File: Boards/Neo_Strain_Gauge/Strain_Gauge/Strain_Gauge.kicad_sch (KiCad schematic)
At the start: 49 parts, among them J1 Screw_Terminal_01x03, J2 Screw_Terminal_01x03, J3 Screw_Terminal_01x03, J4 Screw_Terminal_01x03, J5 Conn_01x02, J6 USB_B_Micro, U1 W25Q128JVS, U2 NCP1117-3.3_SOT223, U3 LTC2344IUH-16-PBF, U4 RP2040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

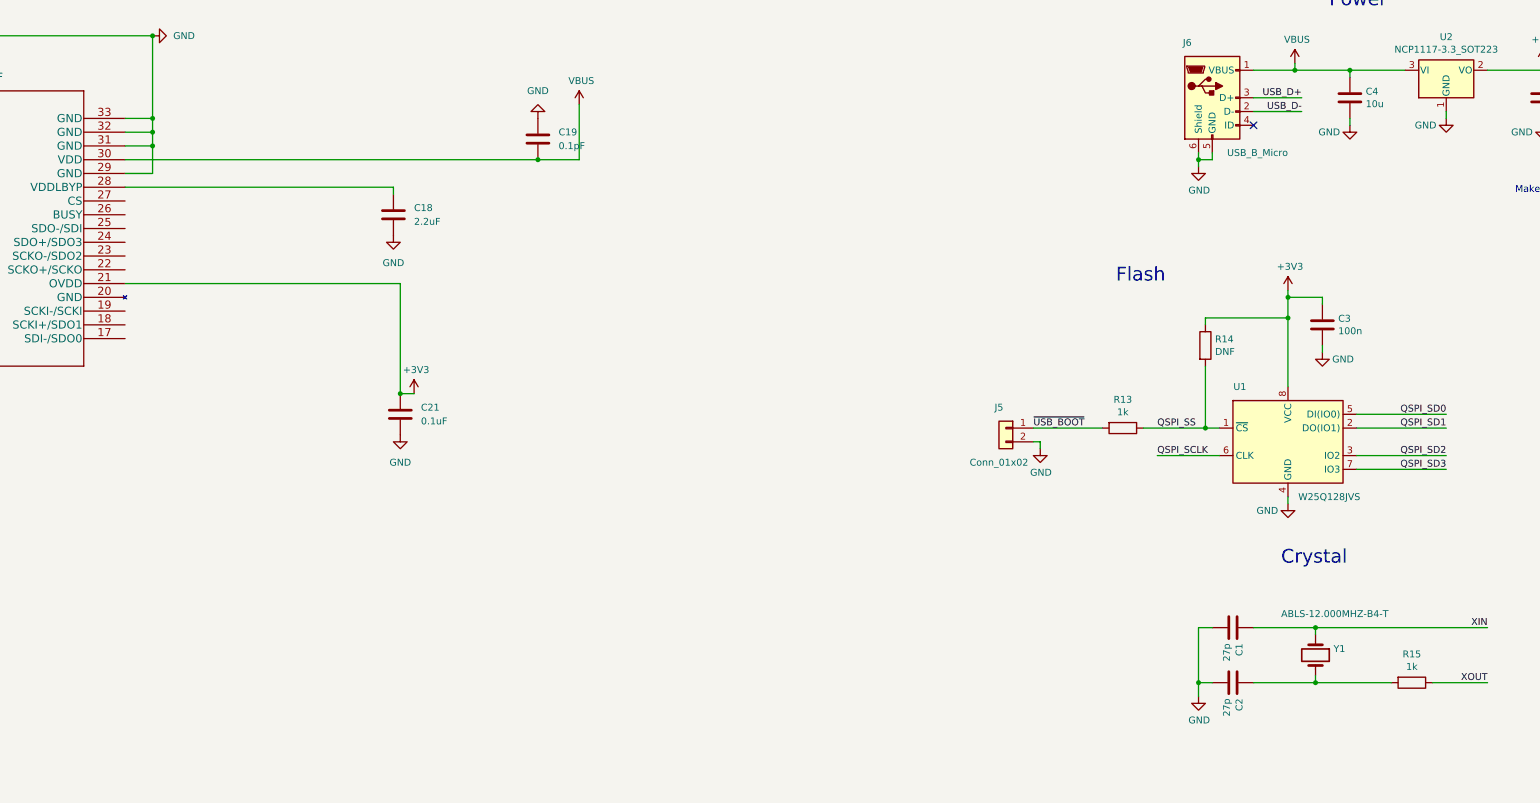
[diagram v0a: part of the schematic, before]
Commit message: Added schematic changes to pull in the mainboard
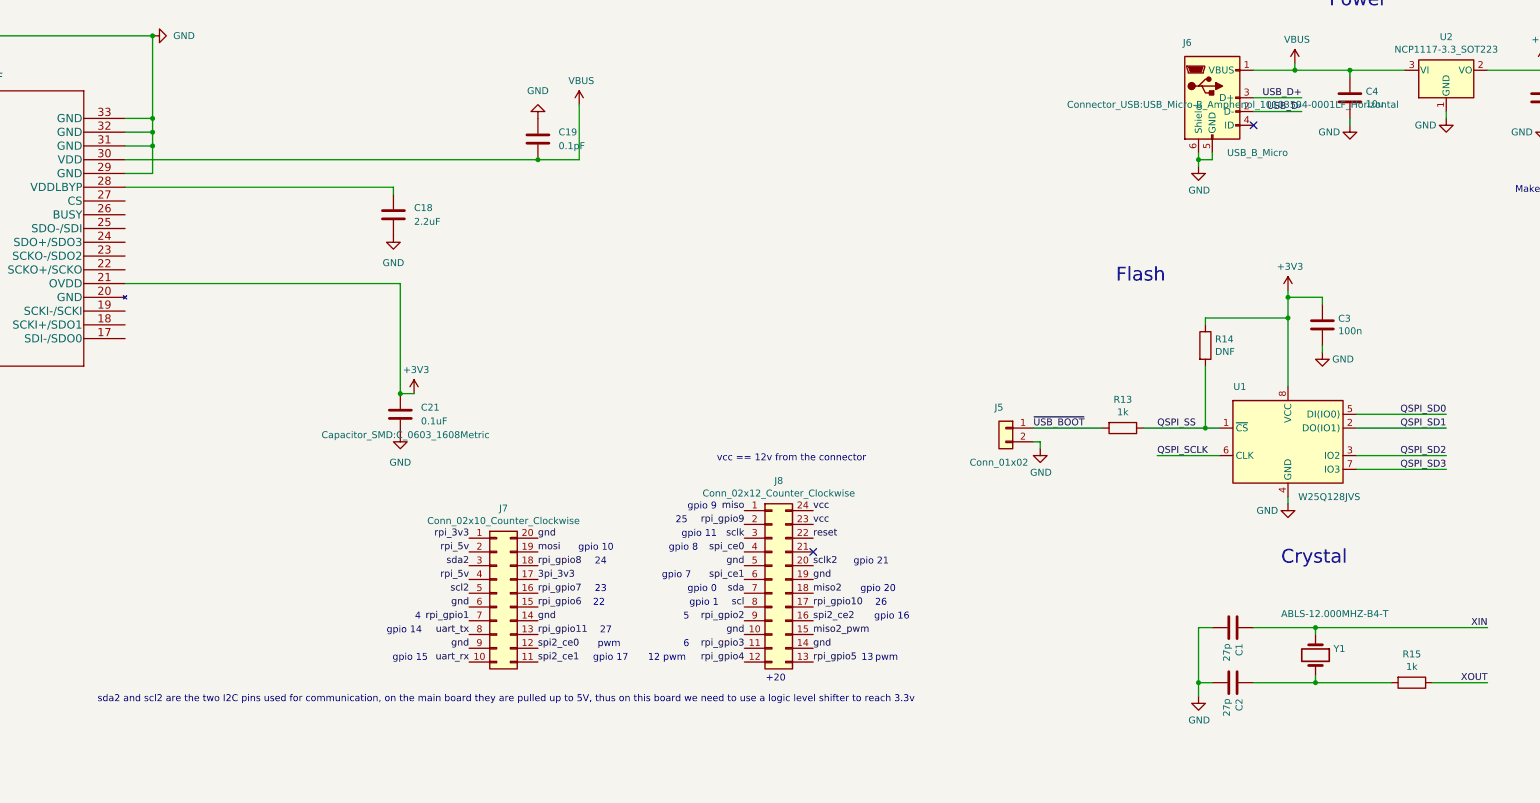
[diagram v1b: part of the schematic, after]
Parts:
- added J7: Conn_02x10_Counter_Clockwise, Connector_PinHeader_2.54mm:PinHeader_2x10_P2.54mm_Vertical, symbol Connector_Generic:Conn_02x10_Counter_Clockwise
- added J8: Conn_02x12_Counter_Clockwise, Connector_PinHeader_2.54mm:PinHeader_2x12_P2.54mm_Vertical, symbol Connector_Generic:Conn_02x12_Counter_Clockwise
- C18, C20: footprint Capacitor_SMD:C_0201_0603Metric -> Capacitor_SMD:C_0603_1608Metric
- C19, C21: footprint (none) -> Capacitor_SMD:C_0603_1608Metric
- J6: footprint RP2040_minimal:USB_Micro-B_Amphenol_10103594-0001LF_Horizontal_modified -> Connector_USB:USB_Micro-B_Amphenol_10103594-0001LF_Horizontal
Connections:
- new net 3pi_3v3: J7.17 (Pin_17)
- new net gnd: J7.14 (Pin_14), J7.20 (Pin_20), J7.6 (Pin_6), J7.9 (Pin_9), J8.10 (Pin_10), J8.14 (Pin_14), J8.19 (Pin_19), J8.5 (Pin_5)
- new net miso: J8.1 (Pin_1)
- new net miso2: J8.18 (Pin_18)
- new net miso2_pwm: J8.15 (Pin_15)
- new net mosi: J7.19 (Pin_19)
- new net reset: J8.22 (Pin_22)
- new net rpi_3v3: J7.1 (Pin_1)
- new net rpi_5v: J7.2 (Pin_2), J7.4 (Pin_4)
- new net rpi_gpio1: J7.7 (Pin_7)
- new net rpi_gpio10: J8.17 (Pin_17)
- new net rpi_gpio11: J7.13 (Pin_13)
- new net rpi_gpio2: J8.9 (Pin_9)
- new net rpi_gpio3: J8.11 (Pin_11)
- new net rpi_gpio4: J8.12 (Pin_12)
- new net rpi_gpio5: J8.13 (Pin_13)
- new net rpi_gpio6: J7.15 (Pin_15)
- new net rpi_gpio7: J7.16 (Pin_16)
- new net rpi_gpio8: J7.18 (Pin_18)
- new net rpi_gpio9: J8.2 (Pin_2)
- new net scl: J8.8 (Pin_8)
- new net scl2: J7.5 (Pin_5)
- new net sclk: J8.3 (Pin_3)
- new net sclk2: J8.20 (Pin_20)
- new net sda: J8.7 (Pin_7)
- new net sda2: J7.3 (Pin_3)
- new net spi2_ce0: J7.12 (Pin_12)
- new net spi2_ce1: J7.11 (Pin_11)
- new net spi2_ce2: J8.16 (Pin_16)
- new net spi_ce0: J8.4 (Pin_4)
- new net spi_ce1: J8.6 (Pin_6)
- new net uart_rx: J7.10 (Pin_10)
- new net uart_tx: J7.8 (Pin_8)
- new net vcc: J8.23 (Pin_23), J8.24 (Pin_24)
- no-connect marks 1 -> 2
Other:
- note added: "+20"
- note added: "12 pwm"
- note added: "13"
- note added: "22"
- note added: "23"
- note added: "24"
- note added: "25"
- note added: "26"
- note added: "27"
- note added: "4"
- note added: "5"
- note added: "6"
- note added: "gpio 0"
- note added: "gpio 1"
- note added: "gpio 10"
- note added: "gpio 11"
- note added: "gpio 14"
- note added: "gpio 15"
- note added: "gpio 16"
- note added: "gpio 17"
- note added: "gpio 20"
- note added: "gpio 21"
- note added: "gpio 7"
- note added: "gpio 8"
- note added: "gpio 9"
- note added: "pwm"
- note added: "sda2 and scl2 are the two I2C pins used for communication, on the main board they are pulled up to 5V, thus on this board we need to use a logic level shifter to reach 3.3v"
- note added: "vcc == 12v from the connector"

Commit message: 0603 more things
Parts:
- C3: footprint Capacitor_SMD:C_0402_1005Metric -> Capacitor_SMD:C_0603_1608Metric
- C4: footprint Capacitor_SMD:C_0805_2012Metric -> Capacitor_SMD:C_0603_1608Metric
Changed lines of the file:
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@@
       (effects (font (size 1.27 1.27)) (justify left))
     )
-    (property "Footprint" "Capacitor_SMD:C_0402_1005Metric" (id 2) (at 247.3452 313.69 0)
+    (property "Footprint" "Capacitor_SMD:C_0603_1608Metric" (id 2) (at 247.3452 313.69 0)
       (effects (font (size 1.27 1.27)) hide)
     )
@@
       (effects (font (size 1.27 1.27)) (justify left))
     )
-    (property "Footprint" "Capacitor_SMD:C_0805_2012Metric" (id 2) (at 252.4252 271.78 0)
+    (property "Footprint" "Capacitor_SMD:C_0603_1608Metric" (id 2) (at 252.4252 271.78 0)
       (effects (font (size 1.27 1.27)) hide)
     )
@@
     )
     (path "/071334f5-4350-4cd7-bf23-5922b5c00fab"
-      (reference "C3") (unit 1) (value "100n") (footprint "Capacitor_SMD:C_0402_1005Metric")
+      (reference "C3") (unit 1) (value "100n") (footprint "Capacitor_SMD:C_0603_1608Metric")
     )
     (path "/d0a1192c-a07d-40a6-a7b0-dc33661cf95a"
-      (reference "C4") (unit 1) (value "10u") (footprint "Capacitor_SMD:C_0805_2012Metric")
+      (reference "C4") (unit 1) (value "10u") (footprint "Capacitor_SMD:C_0603_1608Metric")
     )
     (path "/88bc9d99-afa2-40e7-b578-1b4cda291bf5"

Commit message: Add current work
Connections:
- net GND: now also J7.14 (Pin_14), J7.20 (Pin_20), J7.6 (Pin_6), J8.10 (Pin_10), J8.14 (Pin_14), J8.19 (Pin_19), J8.5 (Pin_5)
- net gnd: no longer J7.14 (Pin_14), J7.20 (Pin_20), J7.6 (Pin_6), J8.10 (Pin_10), J8.14 (Pin_14), J8.19 (Pin_19), J8.5 (Pin_5)
- no-connect marks 2 -> 3
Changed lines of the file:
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@@
   (junction (at -44.45 292.1) (diameter 0) (color 0 0 0 0)
   )
+  (junction (at 124.46 364.49) (diameter 0) (color 0 0 0 0)
+  )
   (junction (at 441.96 264.16) (diameter 0) (color 0 0 0 0)
   )
+  (junction (at 124.46 354.33) (diameter 0) (color 0 0 0 0)
+  )
   (junction (at 223.52 375.92) (diameter 0) (color 0 0 0 0)
   )
@@
   (junction (at 419.1 275.59) (diameter 0) (color 0 0 0 0)
   )
+  (junction (at 167.64 356.87) (diameter 0) (color 0 0 0 0)
+  )
   (junction (at 251.46 262.89) (diameter 0) (color 0 0 0 0)
   )
@@
   )
   (no_connect (at 233.68 273.05))
+  (no_connect (at 707.39 374.65))
   (no_connect (at 152.4 351.79))
   (wire (pts (xy 365.76 297.18) (xy 365.76 284.48))
@@
     (stroke (width 0) (type default) (color 0 0 0 0))
   )
+  (wire (pts (xy 101.6 364.49) (xy 124.46 364.49))
+    (stroke (width 0) (type default) (color 0 0 0 0))
+  )
   (wire (pts (xy 226.06 365.76) (xy 223.52 365.76))
     (stroke (width 0) (type default) (color 0 0 0 0))
@@
     (stroke (width 0) (type default) (color 0 0 0 0))
   )
+  (wire (pts (xy 167.64 356.87) (xy 170.18 356.87))
+    (stroke (width 0) (type default) (color 0 0 0 0))
+  )
   (wire (pts (xy 391.16 358.14) (xy 406.4 358.14))
     (stroke (width 0) (type default) (color 0 0 0 0))
@@
     (stroke (width 0) (type default) (color 0 0 0 0))
   )
+  (wire (pts (xy 101.6 349.25) (xy 116.84 349.25))
+    (stroke (width 0) (type default) (color 0 0 0 0))
+  )
   (wire (pts (xy 359.41 398.78) (xy 359.41 401.32))
     (stroke (width 0) (type default) (color 0 0 0 0))
@@
     (stroke (width 0) (type default) (color 0 0 0 0))
   )
+  (wire (pts (xy 124.46 364.49) (xy 124.46 367.03))
+    (stroke (width 0) (type default) (color 0 0 0 0))
+  )
   (wire (pts (xy -55.88 294.64) (xy -55.88 328.93))
     (stroke (width 0) (type default) (color 0 0 0 0))
@@
     (stroke (width 0) (type default) (color 0 0 0 0))
   )
+  (wire (pts (xy 167.64 369.57) (xy 167.64 356.87))
+    (stroke (width 0) (type default) (color 0 0 0 0))
+  )
   (wire (pts (xy 224.79 309.88) (xy 224.79 308.61))
     (stroke (width 0) (type default) (color 0 0 0 0))
@@
     (stroke (width 0) (type default) (color 0 0 0 0))
   )
+  (wire (pts (xy 124.46 354.33) (xy 124.46 364.49))
+    (stroke (width 0) (type default) (color 0 0 0 0))
+  )
   (wire (pts (xy 223.52 278.13) (xy 223.52 279.4))
     (stroke (width 0) (type default) (color 0 0 0 0))
@@
     (stroke (width 0) (type default) (color 0 0 0 0))
   )
+  (wire (pts (xy 139.7 367.03) (xy 124.46 367.03))
+    (stroke (width 0) (type default) (color 0 0 0 0))
+  )
   (wire (pts (xy -223.52 294.64) (xy -205.74 294.64))
     (stroke (width 0) (type default) (color 0 0 0 0))
@@
     (stroke (width 0) (type default) (color 0 0 0 0))
   )
+  (wire (pts (xy 152.4 356.87) (xy 167.64 356.87))
+    (stroke (width 0) (type default) (color 0 0 0 0))
+  )
   (wire (pts (xy 368.3 284.48) (xy 368.3 297.18))
     (stroke (width 0) (type default) (color 0 0 0 0))
@@
     (stroke (width 0) (type default) (color 0 0 0 0))
   )
+  (wire (pts (xy 88.9 361.95) (xy 63.5 361.95))
+    (stroke (width 0) (type default) (color 0 0 0 0))
+  )
   (wire (pts (xy 391.16 327.66) (xy 406.4 327.66))
     (stroke (width 0) (type default) (color 0 0 0 0))
@@
     (stroke (width 0) (type default) (color 0 0 0 0))
   )
+  (wire (pts (xy 124.46 354.33) (xy 139.7 354.33))
+    (stroke (width 0) (type default) (color 0 0 0 0))
+  )
   (wire (pts (xy 363.22 297.18) (xy 363.22 284.48))
     (stroke (width 0) (type default) (color 0 0 0 0))
@@
     (stroke (width 0) (type default) (color 0 0 0 0))
   )
+  (wire (pts (xy 152.4 369.57) (xy 167.64 369.57))
+    (stroke (width 0) (type default) (color 0 0 0 0))
+  )
   (wire (pts (xy 419.1 264.16) (xy 430.53 264.16))
     (stroke (width 0) (type default) (color 0 0 0 0))
@@
     (stroke (width 0) (type default) (color 0 0 0 0))
   )
+  (wire (pts (xy 63.5 361.95) (xy 63.5 364.49))
+    (stroke (width 0) (type default) (color 0 0 0 0))
+  )
   (wire (pts (xy -217.17 349.25) (xy -217.17 341.63))
     (stroke (width 0) (type default) (color 0 0 0 0))
@@
   )
   (wire (pts (xy -233.68 346.71) (xy -222.25 346.71))
+    (stroke (width 0) (type default) (color 0 0 0 0))
+  )
+  (wire (pts (xy 121.92 354.33) (xy 124.46 354.33))
     (stroke (width 0) (type default) (color 0 0 0 0))
   )
@@
     (effects (font (size 1.27 1.27)) (justify right bottom))
   )
-  (label "gnd" (at 139.7 354.33 180)
-    (effects (font (size 1.27 1.27)) (justify right bottom))
-  )
   (label "GPIO26_ADC0" (at 406.4 383.54 180)
     (effects (font (size 1.27 1.27)) (justify right bottom))
@@
     (effects (font (size 1.27 1.27)) (justify right bottom))
   )
-  (label "gnd" (at 152.4 356.87 0)
-    (effects (font (size 1.27 1.27)) (justify left bottom))
-  )
   (label "GPIO13" (at 406.4 347.98 180)
     (effects (font (size 1.27 1.27)) (justify right bottom))
@@
     (effects (font (size 1.27 1.27)) (justify right bottom))
   )
-  (label "gnd" (at 88.9 361.95 180)
-    (effects (font (size 1.27 1.27)) (justify right bottom))
-  )
   (label "spi2_ce2" (at 152.4 364.49 0)
     (effects (font (size 1.27 1.27)) (justify left bottom))
@@
     (effects (font (size 1.27 1.27)) (justify right bottom))
   )
-  (label "gnd" (at 139.7 367.03 180)
-    (effects (font (size 1.27 1.27)) (justify right bottom))
-  )
   (label "QSPI_SCLK" (at 215.9 334.01 0)
     (effects (font (size 1.27 1.27)) (justify left bottom))
@@
     (effects (font (size 1.27 1.27)) (justify right bottom))
   )
-  (label "gnd" (at 101.6 364.49 0)
-    (effects (font (size 1.27 1.27)) (justify left bottom))
-  )
   (label "rpi_gpio11" (at 101.6 367.03 0)
     (effects (font (size 1.27 1.27)) (justify left bottom))
@@
     (effects (font (size 1.27 1.27)) (justify right bottom))
   )
-  (label "gnd" (at 101.6 349.25 0)
-    (effects (font (size 1.27 1.27)) (justify left bottom))
-  )
   (label "GPIO7" (at 406.4 332.74 180)
     (effects (font (size 1.27 1.27)) (justify right bottom))
@@
   )
   (label "rpi_gpio6" (at 101.6 361.95 0)
-    (effects (font (size 1.27 1.27)) (justify left bottom))
-  )
-  (label "gnd" (at 152.4 369.57 0)
     (effects (font (size 1.27 1.27)) (justify left bottom))
   )
@@
     (pin "1")
     (pin "2")
+  )
+  (symbol (lib_id "power:GND") (at 63.5 364.49 0) (unit 1)
+    (in_bom yes) (on_board yes) (fields_autoplaced)
+    (property "Reference" "#PWR?" (id 0) (at 63.5 370.84 0)
+      (effects (font (size 1.27 1.27)) hide)
+    )
+    (property "Value" "GND" (id 1) (at 63.5 369.57 0))
+    (property "Footprint" "" (id 2) (at 63.5 364.49 0)
+      (effects (font (size 1.27 1.27)) hide)
+    )
+    (property "Datasheet" "" (id 3) (at 63.5 364.49 0)
+      (effects (font (size 1.27 1.27)) hide)
+    )
+    (pin "1")
   )
   (symbol (lib_id "power:GND") (at 76.2 330.2 0) (unit 1)
@@
     (pin "2")
   )
+  (symbol (lib_id "power:GND") (at 121.92 354.33 0) (unit 1)
+    (in_bom yes) (on_board yes) (fields_autoplaced)
+    (property "Reference" "#PWR?" (id 0) (at 121.92 360.68 0)
+      (effects (font (size 1.27 1.27)) hide)
+    )
+    (property "Value" "GND" (id 1) (at 121.92 359.41 0))
+    (property "Footprint" "" (id 2) (at 121.92 354.33 0)
+      (effects (font (size 1.27 1.27)) hide)
+    )
+    (property "Datasheet" "" (id 3) (at 121.92 354.33 0)
+      (effects (font (size 1.27 1.27)) hide)
+    )
+    (pin "1")
+  )
   (symbol (lib_id "power:GND") (at 246.38 314.96 0) (unit 1)
     (in_bom yes) (on_board yes)
@@
     (pin "1")
   )
+  (symbol (lib_id "power:GND") (at 170.18 356.87 0) (unit 1)
+    (in_bom yes) (on_board yes) (fields_autoplaced)
+    (property "Reference" "#PWR?" (id 0) (at 170.18 363.22 0)
+      (effects (font (size 1.27 1.27)) hide)
+    )
+    (property "Value" "GND" (id 1) (at 170.18 361.95 0))
+    (property "Footprint" "" (id 2) (at 170.18 356.87 0)
+      (effects (font (size 1.27 1.27)) hide)
+    )
+    (property "Datasheet" "" (id 3) (at 170.18 356.87 0)
+      (effects (font (size 1.27 1.27)) hide)
+    )
+    (pin "1")
+  )
   (symbol (lib_id "Device:C") (at 287.02 267.97 0) (unit 1)
     (in_bom yes) (on_board yes)
@@
     )
     (property "Datasheet" "" (id 3) (at 427.99 389.89 0)
+      (effects (font (size 1.27 1.27)) hide)
+    )
+    (pin "1")
+  )
+  (symbol (lib_id "power:GND") (at 116.84 349.25 0) (unit 1)
+    (in_bom yes) (on_board yes) (fields_autoplaced)
+    (property "Reference" "#PWR?" (id 0) (at 116.84 355.6 0)
+      (effects (font (size 1.27 1.27)) hide)
+    )
+    (property "Value" "GND" (id 1) (at 116.84 354.33 0))
+    (property "Footprint" "" (id 2) (at 116.84 349.25 0)
+      (effects (font (size 1.27 1.27)) hide)
+    )
+    (property "Datasheet" "" (id 3) (at 116.84 349.25 0)
       (effects (font (size 1.27 1.27)) hide)
     )
@@
       (reference "#PWR0108") (unit 1) (value "GND") (footprint "")
     )
+    (path "/13a05ecb-8a9f-4d56-87f1-21ffdb61c1fe"
+      (reference "#PWR?") (unit 1) (value "GND") (footprint "")
+    )
+    (path "/6040875e-afc2-4303-8054-02fd1d9c2726"
+      (reference "#PWR?") (unit 1) (value "GND") (footprint "")
+    )
+    (path "/87a42555-ed45-45dc-83eb-bba15b903a37"
+      (reference "#PWR?") (unit 1) (value "GND") (footprint "")
+    )
+    (path "/9fb8bffb-8185-4697-a5dc-2efe2256e69f"
+      (reference "#PWR?") (unit 1) (value "GND") (footprint "")
+    )
     (path "/5ada49b8-8e96-4086-b7e6-4acbf8622b7e"

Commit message: PCB Design process should be beginning soon
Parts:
- removed C20: 0.1uF, Capacitor_SMD:C_0603_1608Metric, symbol Device:C
- added C.M.1: 10u, Capacitor_SMD:C_0805_2012Metric, symbol Device:C
- added D1: BAT54C, Package_TO_SOT_SMD:SOT-23, symbol Diode:BAT54C
- added JP2, JP3, JP4, JP5: Jumper_3_Open, Connector_PinHeader_1.00mm:PinHeader_1x03_P1.00mm_Vertical, symbol Jumper:Jumper_3_Open
- added U.M.1: KA78M05_TO252, Package_TO_SOT_SMD:TO-252-2, symbol Regulator_Linear:KA78M05_TO252
- added U5: SN74LV1T34DBV, Package_TO_SOT_SMD:SOT-23-5, symbol Logic_LevelTranslator:SN74LV1T34DBV
- C1, C2, R13, R15: footprint Capacitor_SMD:C_0402_1005Metric -> Capacitor_SMD:C_0603_1608Metric
- C17: value 10u -> 47uF; footprint Capacitor_SMD:C_0805_2012Metric -> Capacitor_SMD:C_0603_1608Metric
- R1, R10, R11, R12, R16, R17, R2, R5, R6, R7, R8, R9: footprint (none) -> Resistor_SMD:R_0805_2012Metric
- U3: footprint UH_32_ADI -> Package_DFN_QFN:QFN-32-1EP_5x5mm_P0.5mm_EP3.45x3.45mm
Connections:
- net +3V3: now also JP2.3 (B), JP3.3 (B), JP4.3 (B), JP5.3 (B), U5.5 (VCC); no longer C17.1
- net GND: now also U3.10 (REFIN), U3.13 (PD), U3.16 (SDI+), U3.20 (GND), C.M.1.2, JP2.1 (A), JP3.1 (A), JP4.1 (A), JP5.1 (A), U.M.1.2 (GND), U5.3 (GND)
- net GPIO10: now also JP4.2 (C)
- net GPIO11: now also JP5.2 (C)
- net GPIO17: now also U3.27 (CS)
- net GPIO18: now also U3.19 (SCKI-/SCKI)
- net GPIO19: now also U3.25 (SDO-/SDI)
- net GPIO23: now also U3.15 (CNV)
- net GPIO24: now also U3.26 (BUSY)
- net GPIO25: now also U3.22 (SCKO+/SCKO)
- net GPIO4: now also U3.17 (SDI-/SDO0)
- net GPIO5: now also U3.18 (SCKI+/SDO1)
- net GPIO6: now also U3.23 (SCKO-/SDO2)
- net GPIO7: now also U3.24 (SDO+/SDO3)
- net GPIO8: now also JP2.2 (C)
- net GPIO9: now also JP3.2 (C)
- net RUN: now also U5.4 (Y)
- net reset: now also U5.2 (A)
- net rpi_5v: now also U.M.1.1 (VI)
- net +5V: now reaches U3.12 (REFBUF)
- net +5V: now also C17.1, C19.2, U3.30 (VDD), C.M.1.1, D1.2, U.M.1.3 (VO)
- removed net VBUS: C19.2, C4.1, J6.1 (VBUS), U2.3 (VI), U3.30 (VDD)
- new net: D1.1, J6.1 (VBUS)
- new net: C4.1, D1.3, U2.3 (VI)
- no-connect marks 3 -> 2

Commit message: Hopefully a good layout for the board
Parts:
- C.M.1, C5: footprint Capacitor_SMD:C_0805_2012Metric -> Capacitor_SMD:C_0603_1608Metric
- J1, J2, J3, J4: footprint (none) -> TerminalBlock:TerminalBlock_Altech_AK300-3_P5.00mm
- J6: footprint Connector_USB:USB_Micro-B_Amphenol_10103594-0001LF_Horizontal -> RP2040_minimal:USB_Micro-B_Amphenol_10103594-0001LF_Horizontal_modified
- JP2, JP3, JP4, JP5: footprint Connector_PinHeader_1.00mm:PinHeader_1x03_P1.00mm_Vertical -> Connector_PinHeader_2.00mm:PinHeader_1x03_P2.00mm_Vertical
- Y1: footprint RP2040_minimal:Crystal_SMD_HC49-US -> Crystal:Crystal_SMD_HC49-SD
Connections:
- net gnd is gone; now on net GND: J7.9 (Pin_9)
- net +5V: now also R1.1, R11.1, R16.1, R17.1, R2.1, R5.1, R7.1, R9.1
- net GPIO15: now also U3.27 (CS)
- net GPIO17: no longer U3.27 (CS)
- net USB_DR-: now reaches R4.2, U4.46 (USB_DM)
- net USB_DR+: now reaches R3.2, U4.47 (USB_DP)

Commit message: Update to latest schematic and board design slots.
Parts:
- C21: value 0.1uF -> 100n
- R1, R10, R11, R12, R16, R17, R2, R5, R6, R7, R8, R9: Purchase Link (none) -> https://www.digikey.com/en/products/detail/vishay-foil-resi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
- renumbered C.M.1 to C20, U.M.1 to U6
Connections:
- net GND: now also J1.1 (Pin_1), J2.1 (Pin_1), J3.1 (Pin_1), J4.1 (Pin_1), R10.2, R12.2, R6.2, R8.2
